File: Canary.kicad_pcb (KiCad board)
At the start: 4 copper layers, 56 x 38 mm, 82 parts, among them J1 CONN_ARM_CM_JTAG_SWD_10, J2 BMD-300-A-R, J3 CONN_20021311-00010T4LF_AMP, J4 USB4125-GF-A, J5 S2B-PH-SM4-TB, Q1 PMN30UNX, Q2 PMN42XPEAH, Q3 PMN30UNX, SW1 TL3301SPF160QJ, U1 DNP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

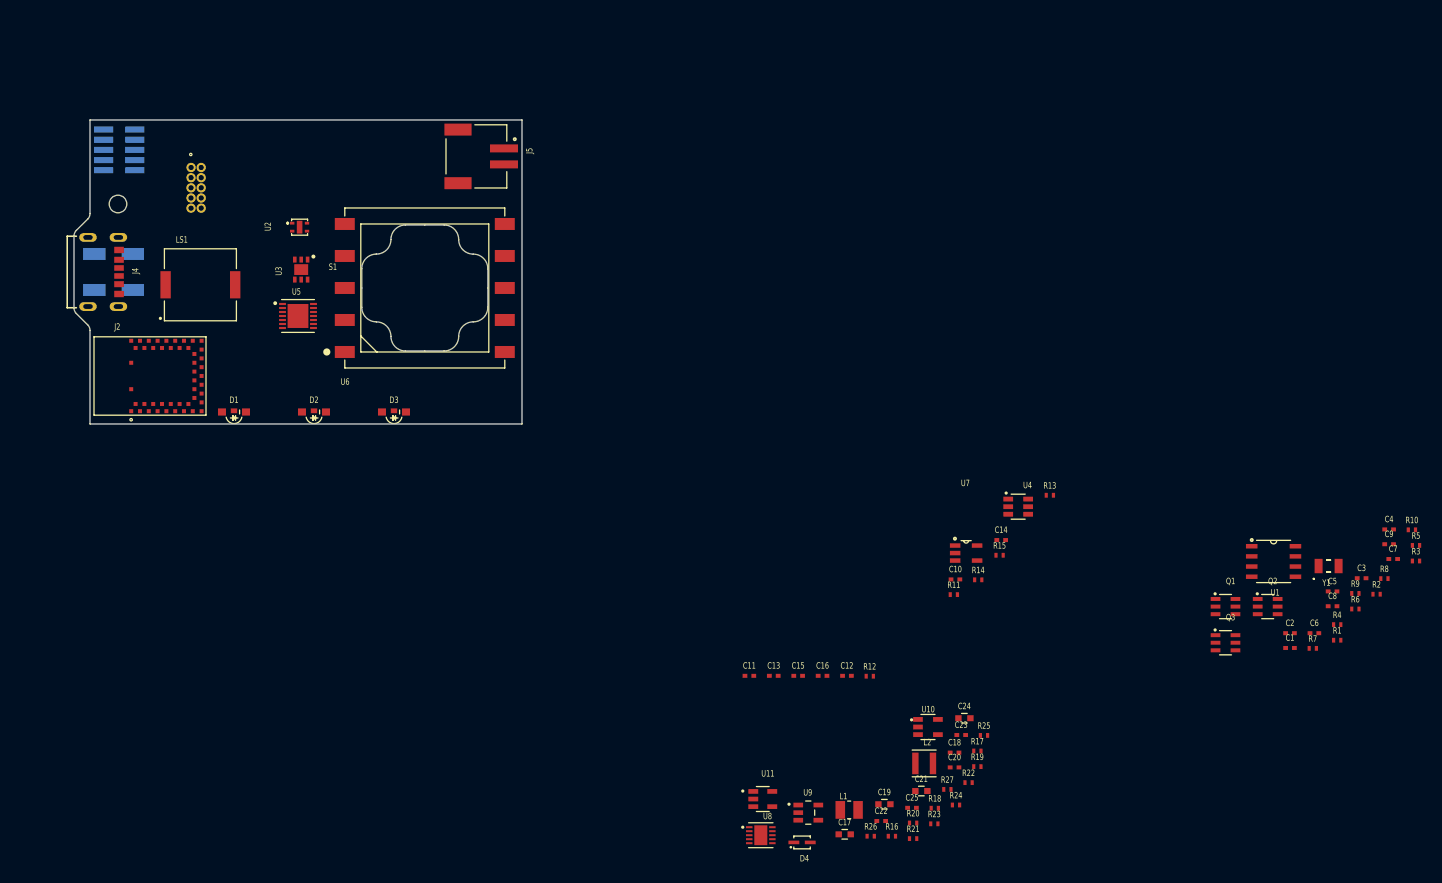
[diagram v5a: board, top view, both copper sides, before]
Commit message: group components
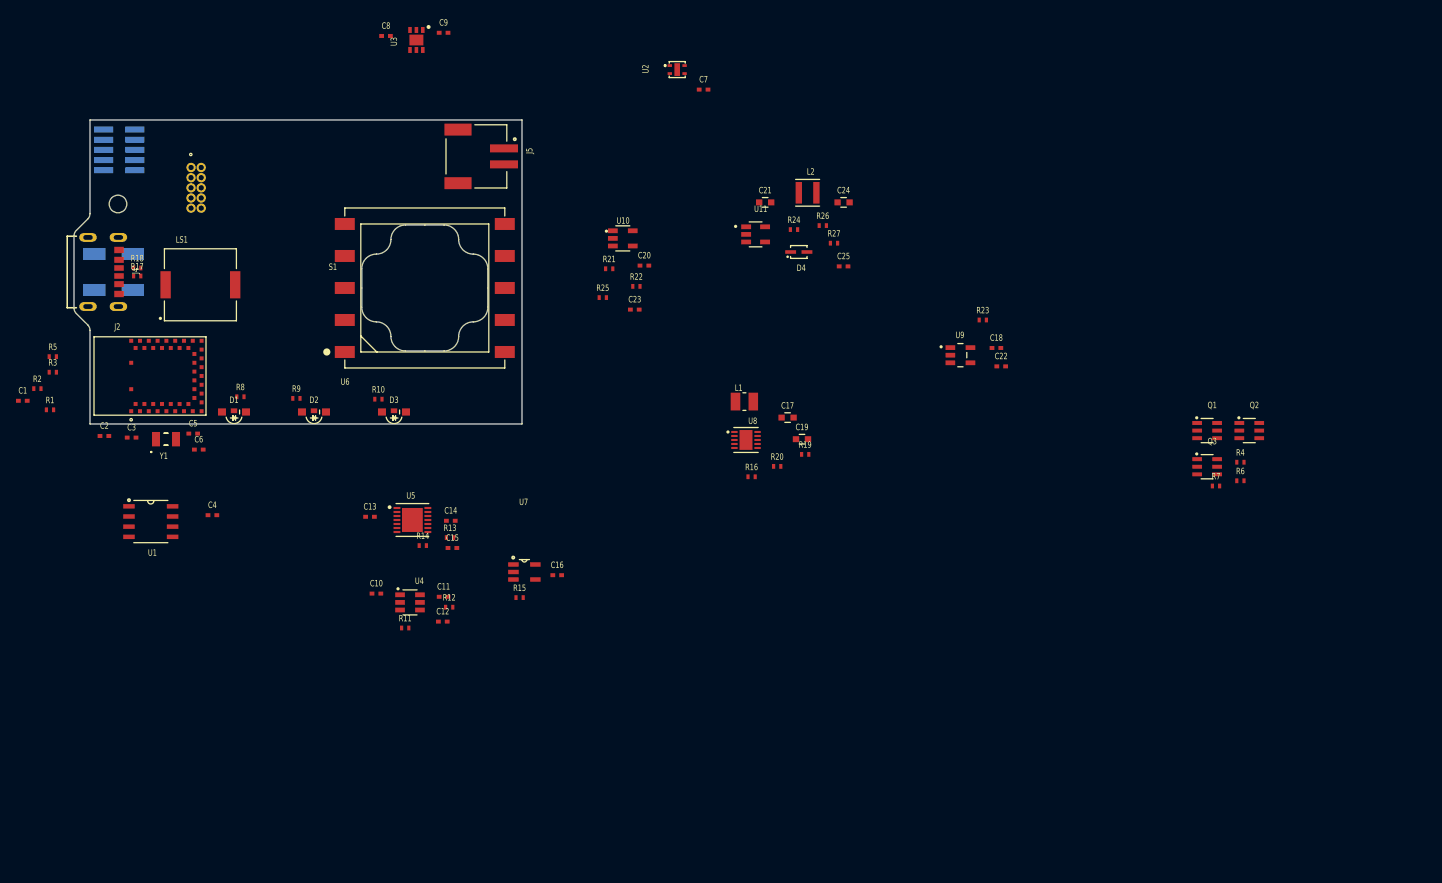
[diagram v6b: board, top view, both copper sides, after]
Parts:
- moved R3 172.0 mm to (38.4, 79.5)
- moved R5 172.0 mm to (38.4, 77.6)
- moved R2 169.4 mm to (36.4, 81.6)
- moved R1 163.5 mm to (38.0, 84.2)
- moved C1 161.4 mm to (34.6, 83.1)
- moved C3 154.8 mm to (48.2, 87.7)
- moved C2 150.2 mm to (44.8, 87.5)
- moved C4 147.1 mm to (58.3, 97.4)
- moved Y1 146.2 mm to (52.5, 87.9)
- moved R8 144.8 mm to (61.8, 82.6)
- moved C5 143.8 mm to (55.9, 87.2)
- moved C6 141.3 mm to (56.6, 89.2)
- moved U1 140.4 mm to (50.6, 98.2)
- moved C8 138.1 mm to (80.0, 37.5)
- moved R9 134.6 mm to (68.8, 82.8)
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
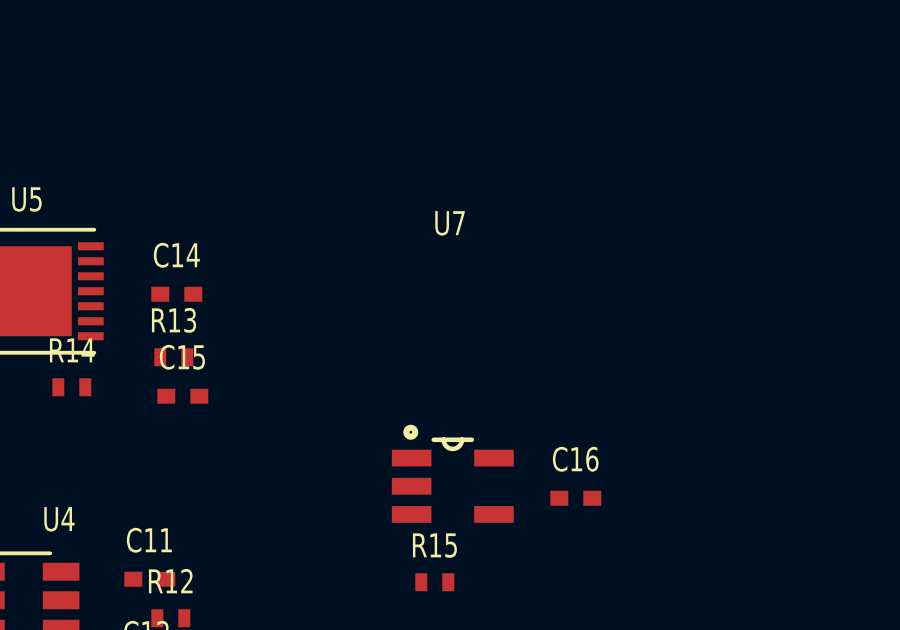
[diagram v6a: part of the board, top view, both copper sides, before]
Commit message: Clean up schem, wire in button
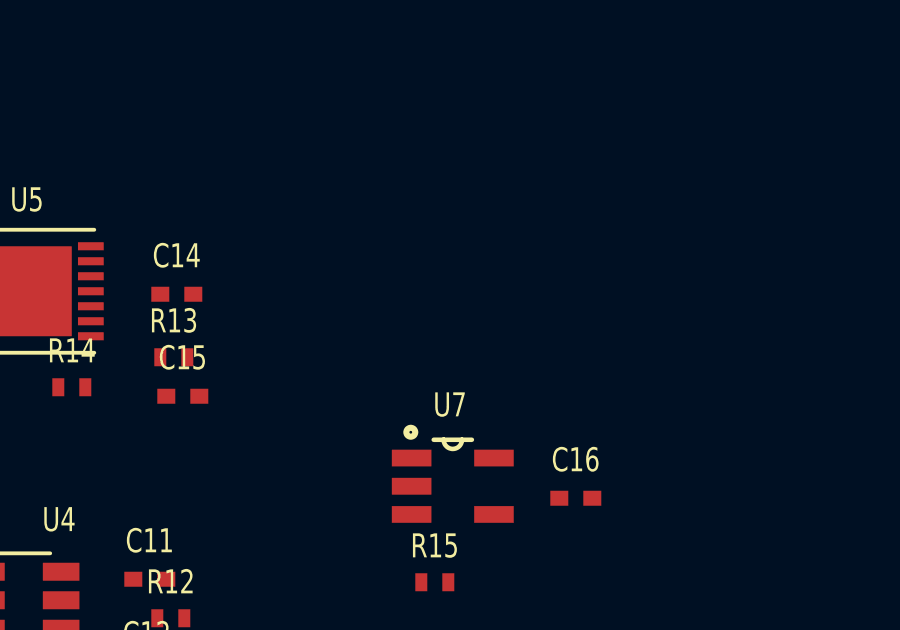
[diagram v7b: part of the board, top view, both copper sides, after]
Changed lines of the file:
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@@
   (module JetkovKiCADLib:MCP6041T-I_OT (layer F.Cu)
     (at 97.3 104.5)
-    (fp_text reference U7 (at -0.09329 -8.7407) (layer F.SilkS)
+    (fp_text reference U7 (at -0.09329 -2.7) (layer F.SilkS)
       (effects (font (size 0.8 0.6) (thickness 0.15)))
     )

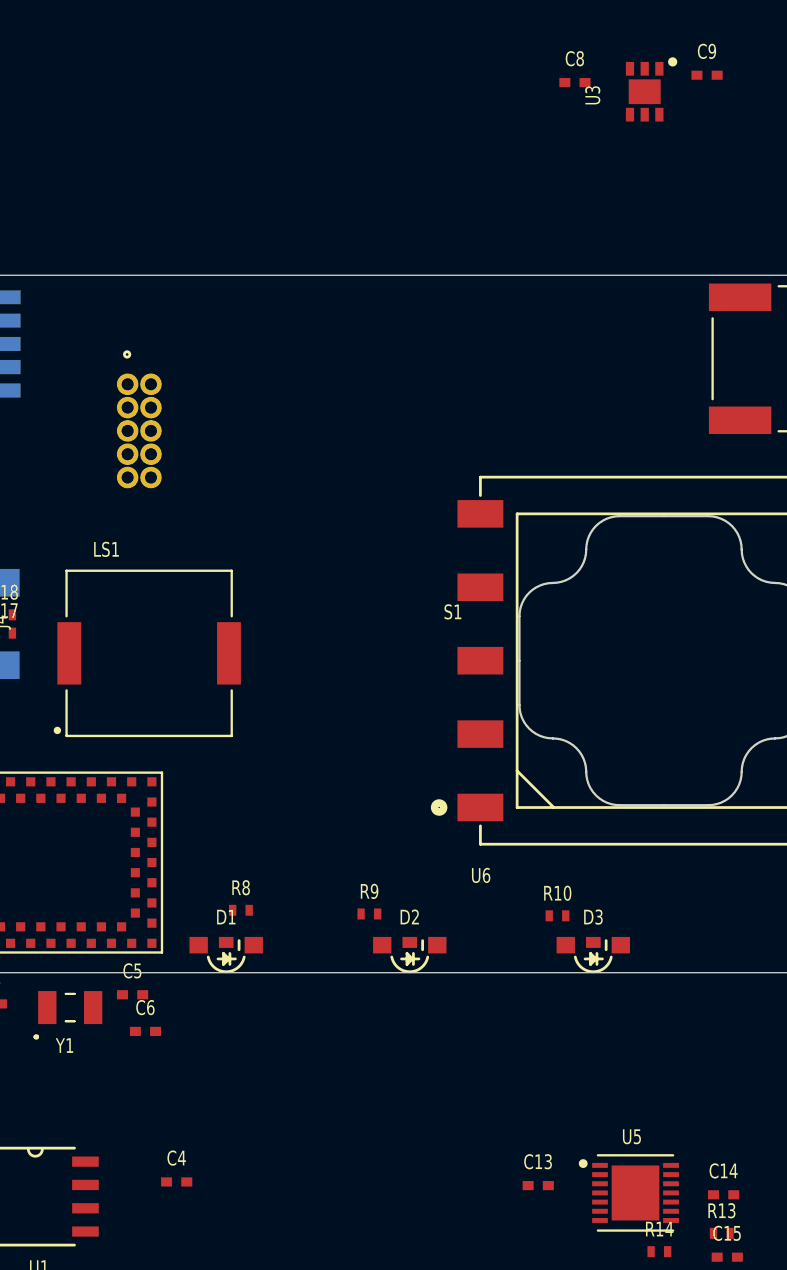
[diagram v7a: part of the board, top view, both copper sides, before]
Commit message: Review everything, ready for layout
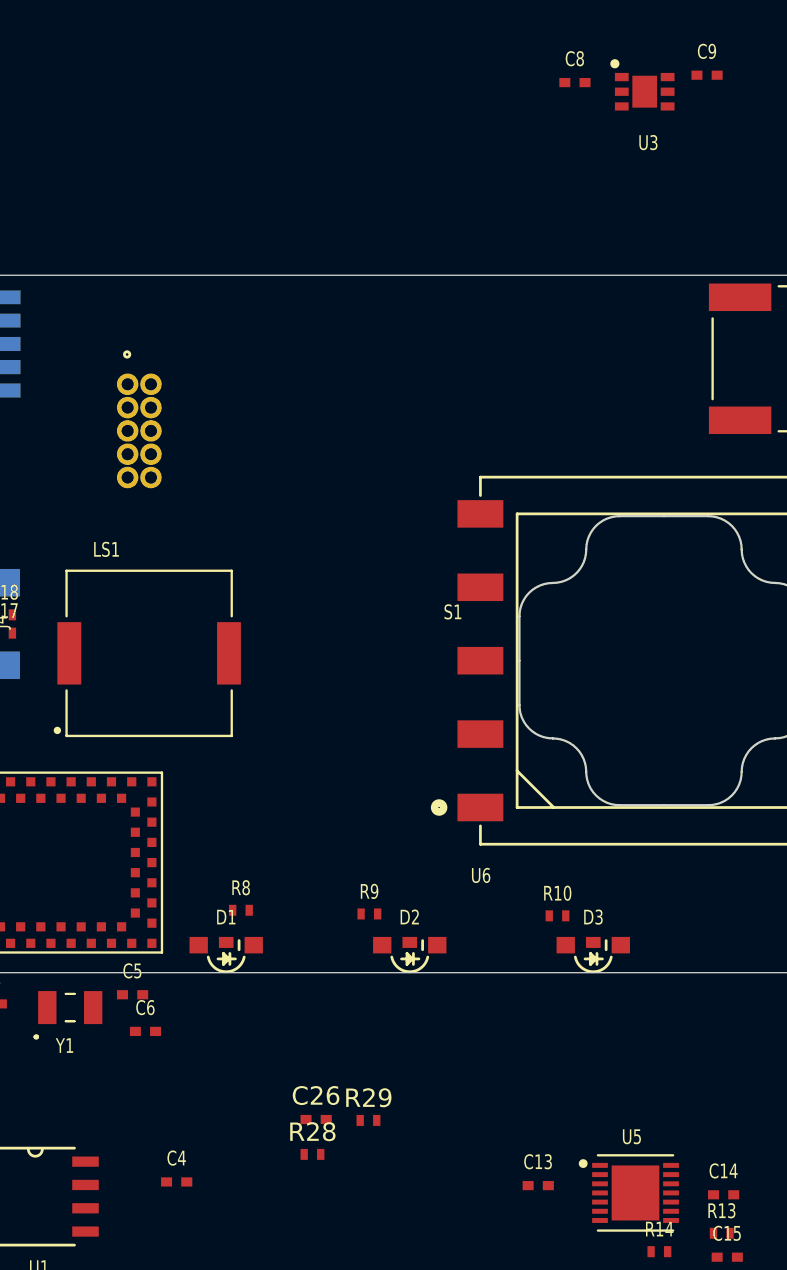
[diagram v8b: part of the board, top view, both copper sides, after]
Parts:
- added C26: 0.1u, JetkovKiCADLib:C_0402_NoSilk, F.Cu at (65.9, 94.0)
- added R28: 100k, JetkovKiCADLib:R_0402_NoSilk, F.Cu at (65.7, 95.9)
- added R29: 100k, JetkovKiCADLib:R_0402_NoSilk, F.Cu at (68.8, 94.0)
- J3: value CONN_20021311-00010T4LF_AMP -> 20021311-00010T4LF
- R10: value ? -> 500R
- R21: value 330k -> 300k
- R8, R9: value ? -> 470R
- turned U3 to 0 degrees
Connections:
- net Net-(C15-Pad1) renamed /Potentiostat/FILT_C2
- net Net-(C15-Pad2) renamed /Potentiostat/FILT_C1
- net Net-(Q2-Pad3) renamed /PG
- net Net-(Q3-Pad3) renamed /NG
- net Net-(R14-Pad1) renamed /Potentiostat/SPEC_CE
- net Net-(R14-Pad2) renamed /Potentiostat/CE
- net Net-(U5-Pad12) renamed /Potentiostat/SPEC_WE
- net Net-(U5-Pad13) renamed /Potentiostat/SPEC_RE
- J2 pad 10: LED_AMBER -> (no net)
- J2 pad 11: LED_GREEN -> (no net)
- J2 pad 22: (no net) -> LED_RED
- J2 pad 23: (no net) -> LED_AMBER
- J2 pad 24: (no net) -> LED_GREEN
- J2 pad 37: (no net) -> BUTTON
- J2 pad 38: (no net) -> ~PM_RST~
- J2 pad 9: LED_RED -> (no net)
- J3 pad 5: (no net) -> ~PM_RST~
- SW1 pad 1: (no net) -> +3V3
- SW1 pad 2: (no net) -> +3V3
- SW1 pad 3: (no net) -> /RBTN
- SW1 pad 4: (no net) -> /RBTN
- U2 pad 2: GND -> I2C_SCL
- U2 pad 4: (no net) -> GND
- U2 pad 5: I2C_SCL -> GND
